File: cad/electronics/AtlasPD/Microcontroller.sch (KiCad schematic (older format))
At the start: 23 parts, among them J2 USB_C_Receptacle_USB2.0, SW1 SW_MEC_5E, U2 ATmega328P-AU, U4 CP2104, Y1 CSTNE16M0V53-R0

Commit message: Started layout
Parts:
- removed SW1: SW_MEC_5E, Button_Switch_SMD:SW_Push_1P1T_NO_6x6mm_H9.5mm, symbol Switch:SW_MEC_5E
- added R12: 0, Resistor_SMD:R_0603_1608Metric, symbol Device:R_Small
- added SW1: SW_SPST, Button_Switch_SMD:SW_Push_1P1T_NO_6x6mm_H9.5mm, symbol Switch:SW_SPST
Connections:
- wire segments 121 -> 117
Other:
- moved on the sheet: R4, R5
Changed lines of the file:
@@
 NoConn ~ 1050 2800
 Wire Wire Line
-	1950 1800 2100 1800
-Wire Wire Line
-	2100 1800 2100 1900
-Wire Wire Line
 	2100 1900 1950 1900
 Wire Wire Line
@@
 Wire Wire Line
 	2100 2100 1950 2100
-Text Label 2450 1800 2    50   ~ 0
+Text Label 2750 1800 2    50   ~ 0
 USB_DN
 Text Label 2450 2000 2    50   ~ 0
 USB_DP
-Wire Wire Line
-	2450 1800 2100 1800
-Connection ~ 2100 1800
 Wire Wire Line
 	2450 2000 2100 2000
@@
 L Device:R_Small R5
 U 1 1 6160033E
-P 2300 1600
-F 0 "R5" V 2300 1600 50  0000 C CNN
-F 1 "5.11K" V 2350 1800 50  0000 C CNN
-F 2 "Resistor_SMD:R_0603_1608Metric" H 2300 1600 50  0001 C CNN
-F 3 "~" H 2300 1600 50  0001 C CNN
-	1    2300 1600
+P 2550 1600
+F 0 "R5" V 2550 1600 50  0000 C CNN
+F 1 "5.11K" V 2600 1800 50  0000 C CNN
+F 2 "Resistor_SMD:R_0603_1608Metric" H 2550 1600 50  0001 C CNN
+F 3 "~" H 2550 1600 50  0001 C CNN
+	1    2550 1600
 	0    1    1    0
 $EndComp
@@
 L Device:R_Small R4
 U 1 1 61600F72
-P 2300 1500
-F 0 "R4" V 2300 1500 50  0000 C CNN
-F 1 "5.11K" V 2250 1700 50  0000 C CNN
-F 2 "Resistor_SMD:R_0603_1608Metric" H 2300 1500 50  0001 C CNN
-F 3 "~" H 2300 1500 50  0001 C CNN
-	1    2300 1500
+P 2550 1500
+F 0 "R4" V 2550 1500 50  0000 C CNN
+F 1 "5.11K" V 2500 1700 50  0000 C CNN
+F 2 "Resistor_SMD:R_0603_1608Metric" H 2550 1500 50  0001 C CNN
+F 3 "~" H 2550 1500 50  0001 C CNN
+	1    2550 1500
 	0    1    1    0
 $EndComp
 Wire Wire Line
-	1950 1500 2200 1500
-Wire Wire Line
-	1950 1600 2200 1600
-Wire Wire Line
-	2400 1600 2650 1600
-Wire Wire Line
-	2650 1600 2650 1500
-Wire Wire Line
-	2650 1500 2400 1500
+	2650 1600 2900 1600
+Wire Wire Line
+	2900 1600 2900 1500
+Wire Wire Line
+	2900 1500 2650 1500
 $Comp
 L power:GND #PWR010
 U 1 1 616032B8
-P 2650 1650
-F 0 "#PWR010" H 2650 1400 50  0001 C CNN
-F 1 "GND" H 2655 1477 50  0000 C CNN
-F 2 "" H 2650 1650 50  0001 C CNN
-F 3 "" H 2650 1650 50  0001 C CNN
-	1    2650 1650
-	1    0    0    -1
-$EndComp
-Wire Wire Line
-	2650 1650 2650 1600
-Connection ~ 2650 1600
+P 2900 1650
+F 0 "#PWR010" H 2900 1400 50  0001 C CNN
+F 1 "GND" H 2905 1477 50  0000 C CNN
+F 2 "" H 2900 1650 50  0001 C CNN
+F 3 "" H 2900 1650 50  0001 C CNN
+	1    2900 1650
+	1    0    0    -1
+$EndComp
+Wire Wire Line
+	2900 1650 2900 1600
+Connection ~ 2900 1600
 NoConn ~ 5100 1000
 NoConn ~ 4200 2300
@@
 TXD
 Text Label 5900 1900 2    50   ~ 0
-TXD
+RXD
 Wire Wire Line
 	5600 1500 5900 1500
@@
 	8650 1550 8800 1550
 $Comp
-L Switch:SW_MEC_5E SW1
-U 1 1 616F3B46
-P 10350 3050
-F 0 "SW1" H 10350 3100 50  0000 C CNN
-F 1 "SW_MEC_5E" H 10750 3200 50  0000 C CNN
-F 2 "Button_Switch_SMD:SW_Push_1P1T_NO_6x6mm_H9.5mm" H 10350 3350 50  0001 C CNN
-F 3 "http://www.apem.com/int/index.php?controller=attachment&id_attachment=1371" H 10350 3350 50  0001 C CNN
-	1    10350 3050
-	1    0    0    -1
-$EndComp
-$Comp
 L Device:Resonator_Small Y1
 U 1 1 616F5A36
@@
 $EndComp
 Wire Wire Line
-	8700 2250 9650 2250
-Wire Wire Line
 	8650 2150 9550 2150
 Wire Wire Line
@@
 Wire Wire Line
 	10550 3050 10700 3050
-Wire Wire Line
-	10550 2950 10700 2950
-Wire Wire Line
-	10700 2950 10700 3050
-Connection ~ 10700 3050
 $Comp
 L Device:R_Small R11
@@
 	-1   0    0    1
 $EndComp
-Wire Wire Line
-	10150 2950 10050 2950
-Wire Wire Line
-	10050 2950 10050 3050
-Connection ~ 10050 3050
-Wire Wire Line
-	10050 3050 10150 3050
 $Comp
 L Device:C_Small C11
@@
 	9850 2900 9850 3050
 Connection ~ 9850 3050
-Wire Wire Line
-	9850 3050 10050 3050
 Wire Wire Line
 	9650 2900 9650 3050
@@
 Wire Wire Line
 	8250 1200 8250 1250
+$Comp
+L Switch:SW_SPST SW1
+U 1 1 61815A6D
+P 10350 3050
+F 0 "SW1" H 10350 3000 50  0000 C CNN
+F 1 "SW_SPST" H 10350 3194 50  0000 C CNN
+F 2 "Button_Switch_SMD:SW_Push_1P1T_NO_6x6mm_H9.5mm" H 10350 3050 50  0001 C CNN
+F 3 "~" H 10350 3050 50  0001 C CNN
+	1    10350 3050
+	1    0    0    -1
+$EndComp
+Wire Wire Line
+	9850 3050 10150 3050
+$Comp
+L Device:R_Small R12
+U 1 1 6182599D
+P 2200 1900
+F 0 "R12" V 2200 1900 50  0000 C CNN
+F 1 "0" V 2150 1800 50  0000 C CNN
+F 2 "Resistor_SMD:R_0603_1608Metric" H 2200 1900 50  0001 C CNN
+F 3 "~" H 2200 1900 50  0001 C CNN
+	1    2200 1900
+	0    1    1    0
+$EndComp
+Wire Wire Line
+	1950 1800 2450 1800
+Wire Wire Line
+	2300 1900 2450 1900
+Wire Wire Line
+	2450 1900 2450 1800
+Wire Wire Line
+	2450 1800 2750 1800
+Connection ~ 2450 1800
+Wire Wire Line
+	1950 1500 2450 1500
+Wire Wire Line
+	1950 1600 2450 1600
+Wire Wire Line
+	8650 2250 9650 2250
 $EndSCHEMATC

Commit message: Layout updates, new PMICs for motors
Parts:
- D3, D4, D5, D6: footprint Capacitor_SMD:C_0603_1608Metric -> LED_SMD:LED_0603_1608Metric
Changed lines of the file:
@@
 F 0 "D4" V 3496 1930 50  0000 R CNN
 F 1 "RED" V 3405 1930 50  0000 R CNN
-F 2 "Capacitor_SMD:C_0603_1608Metric" V 3450 2000 50  0001 C CNN
+F 2 "LED_SMD:LED_0603_1608Metric" V 3450 2000 50  0001 C CNN
 F 3 "~" V 3450 2000 50  0001 C CNN
 	1    3450 2000
@@
 F 0 "D3" V 3250 2250 50  0000 R CNN
 F 1 "RED" V 3150 2250 50  0000 R CNN
-F 2 "Capacitor_SMD:C_0603_1608Metric" V 3300 2100 50  0001 C CNN
+F 2 "LED_SMD:LED_0603_1608Metric" V 3300 2100 50  0001 C CNN
 F 3 "~" V 3300 2100 50  0001 C CNN
 	1    3300 2100
@@
 F 0 "D5" V 4789 5132 50  0000 R CNN
 F 1 "YELLOW" V 4698 5132 50  0000 R CNN
-F 2 "Capacitor_SMD:C_0603_1608Metric" H 4750 5250 50  0001 C CNN
+F 2 "LED_SMD:LED_0603_1608Metric" H 4750 5250 50  0001 C CNN
 F 3 "~" H 4750 5250 50  0001 C CNN
 	1    4750 5250
@@
 F 0 "D6" V 5489 5132 50  0000 R CNN
 F 1 "GREEN" V 5398 5132 50  0000 R CNN
-F 2 "Capacitor_SMD:C_0603_1608Metric" H 5450 5250 50  0001 C CNN
+F 2 "LED_SMD:LED_0603_1608Metric" H 5450 5250 50  0001 C CNN
 F 3 "~" H 5450 5250 50  0001 C CNN
 	1    5450 5250

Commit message: Found a bug, squashed it
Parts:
- added J1: Barrel_Jack_MountingPin, Connector_BarrelJack:BarrelJack_Horizontal, symbol Connector:Barrel_Jack_MountingPin
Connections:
- net labels added: EN_MTRS
- wire segments 117 -> 122
- no-connect marks 16 -> 17
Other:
- note added: "ATMEGA328P Microcontroller"
- note added: "DC Barrel Jack 5V Input"
- note added: "Design Block Interconnects"
- note added: "IO Voltage Level Selector"
- note added: "Status LEDs"
- note added: "USB Type-C Connector"
- note added: "USB to UART Serial Bridge"
- moved on the sheet: C6, C7, D3, D4, D5, D6, JP1, R6, R7, R8, R9, U4

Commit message: First Board Layout done
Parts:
- removed J1: Barrel_Jack_MountingPin, Connector_BarrelJack:BarrelJack_Horizontal, symbol Connector:Barrel_Jack_MountingPin
- added J1: Conn_01x04, Connector_JST:JST_PH_B4B-PH-K_1x04_P2.00mm_Vertical, symbol Connector_Generic:Conn_01x04
- renumbered C7 to C1, C6 to C2, C9 to C3, C10 to C4, C11 to C5, D5 to D1, D3 to D2, D4 to D3, D6 to D4, R12 to R1, R4 to R2, R5 to R3, R8 to R4, R6 to R5, R7 to R6, R9 to R7, R10 to R8, R11 to R9, U4 to U1
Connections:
- net labels added: +BATT
- wire segments 122 -> 130
- no-connect marks 17 -> 16
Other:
- note added: "Power Port"
- note removed: "DC Barrel Jack 5V Input"
- moved on the sheet: C3, C4

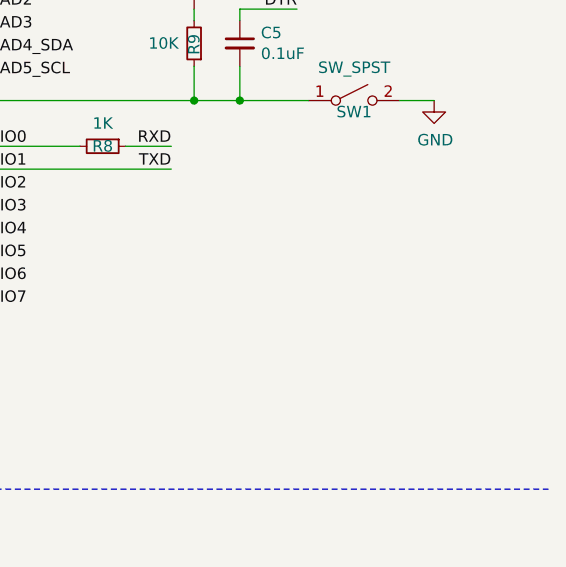
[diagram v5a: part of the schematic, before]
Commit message: Additional layout chaneges, and added testpoints
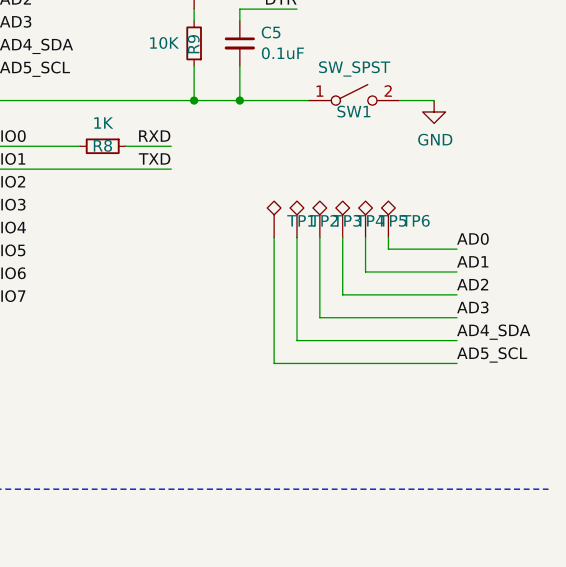
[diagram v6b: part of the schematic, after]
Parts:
- added TP1, TP2, TP3, TP4, TP5, TP6: TestPoint_Alt, TestPoint:TestPoint_Pad_D1.0mm, symbol Connector:TestPoint_Alt
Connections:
- net AD0: now also TP6.1
- net AD1: now also TP5.1
- net AD2: now also TP4.1
- net AD3: now also TP3.1
- net AD4_SDA: now also TP2.1
- net AD5_SCL: now also TP1.1
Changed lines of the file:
@@
 	8800 1200 8650 1200
 NoConn ~ 1050 2800
+$Comp
+L Connector:TestPoint_Alt TP1
+U 1 1 617127E7
+P 10000 3650
+F 0 "TP1" H 10058 3722 50  0000 L CNN
+F 1 "TestPoint_Alt" H 10058 3677 50  0001 L CNN
+F 2 "TestPoint:TestPoint_Pad_D1.0mm" H 10200 3650 50  0001 C CNN
+F 3 "~" H 10200 3650 50  0001 C CNN
+	1    10000 3650
+	1    0    0    -1
+$EndComp
+$Comp
+L Connector:TestPoint_Alt TP2
+U 1 1 61713F79
+P 10100 3650
+F 0 "TP2" H 10158 3722 50  0000 L CNN
+F 1 "TestPoint_Alt" H 10158 3677 50  0001 L CNN
+F 2 "TestPoint:TestPoint_Pad_D1.0mm" H 10300 3650 50  0001 C CNN
+F 3 "~" H 10300 3650 50  0001 C CNN
+	1    10100 3650
+	1    0    0    -1
+$EndComp
+$Comp
+L Connector:TestPoint_Alt TP3
+U 1 1 61714148
+P 10200 3650
+F 0 "TP3" H 10258 3722 50  0000 L CNN
+F 1 "TestPoint_Alt" H 10258 3677 50  0001 L CNN
+F 2 "TestPoint:TestPoint_Pad_D1.0mm" H 10400 3650 50  0001 C CNN
+F 3 "~" H 10400 3650 50  0001 C CNN
+	1    10200 3650
+	1    0    0    -1
+$EndComp
+$Comp
+L Connector:TestPoint_Alt TP4
+U 1 1 61714471
+P 10300 3650
+F 0 "TP4" H 10358 3722 50  0000 L CNN
+F 1 "TestPoint_Alt" H 10358 3677 50  0001 L CNN
+F 2 "TestPoint:TestPoint_Pad_D1.0mm" H 10500 3650 50  0001 C CNN
+F 3 "~" H 10500 3650 50  0001 C CNN
+	1    10300 3650
+	1    0    0    -1
+$EndComp
+$Comp
+L Connector:TestPoint_Alt TP5
+U 1 1 61714782
+P 10400 3650
+F 0 "TP5" H 10458 3722 50  0000 L CNN
+F 1 "TestPoint_Alt" H 10458 3677 50  0001 L CNN
+F 2 "TestPoint:TestPoint_Pad_D1.0mm" H 10600 3650 50  0001 C CNN
+F 3 "~" H 10600 3650 50  0001 C CNN
+	1    10400 3650
+	1    0    0    -1
+$EndComp
+$Comp
+L Connector:TestPoint_Alt TP6
+U 1 1 617149A7
+P 10500 3650
+F 0 "TP6" H 10558 3722 50  0000 L CNN
+F 1 "TestPoint_Alt" H 10558 3677 50  0001 L CNN
+F 2 "TestPoint:TestPoint_Pad_D1.0mm" H 10700 3650 50  0001 C CNN
+F 3 "~" H 10700 3650 50  0001 C CNN
+	1    10500 3650
+	1    0    0    -1
+$EndComp
+Text Label 10800 4200 0    50   ~ 0
+AD5_SCL
+Text Label 10800 4100 0    50   ~ 0
+AD4_SDA
+Text Label 10800 4000 0    50   ~ 0
+AD3
+Text Label 10800 3900 0    50   ~ 0
+AD2
+Text Label 10800 3800 0    50   ~ 0
+AD1
+Text Label 10800 3700 0    50   ~ 0
+AD0
+Wire Wire Line
+	10500 3650 10500 3700
+Wire Wire Line
+	10500 3700 10800 3700
+Wire Wire Line
+	10400 3650 10400 3800
+Wire Wire Line
+	10400 3800 10800 3800
+Wire Wire Line
+	10300 3650 10300 3900
+Wire Wire Line
+	10300 3900 10800 3900
+Wire Wire Line
+	10200 4000 10200 3650
+Wire Wire Line
+	10200 4000 10800 4000
+Wire Wire Line
+	10100 3650 10100 4100
+Wire Wire Line
+	10100 4100 10800 4100
+Wire Wire Line
+	10000 4200 10000 3650
+Wire Wire Line
+	10000 4200 10800 4200
 $EndSCHEMATC

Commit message: Layout updates
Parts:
- added TP207, TP208, TP209, TP210, TP211, TP212: TestPoint_Alt, TestPoint:TestPoint_Pad_D1.0mm, symbol Connector:TestPoint_Alt
- renumbered C1 to C201, C2 to C202, C3 to C203, C4 to C204, C5 to C205, D1 to D201, D2 to D202, D3 to D203, D4 to D204, J2 to J201, J1 to J202, JP1 to JP201, R1 to R201, R2 to R202, R3 to R203, R4 to R204, R5 to R205, R6 to R206, R7 to R207, R8 to R208, R9 to R209, SW1 to SW201, TP1 to TP201, TP2 to TP202, TP3 to TP203, TP4 to TP204, TP5 to TP205, TP6 to TP206, U1 to U201, U2 to U202, Y1 to Y201
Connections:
- net EN_MTRS: now also TP209.1
- net GND: now also TP207.1
- net IO12_MISO: now also TP210.1
- net S4: now also TP211.1
- net VCC: now also TP212.1
- net RESET: now reaches C205.2, R209.1, SW201.1 (A), U202.29 (~RESET~/PC6)
- net RESET: now also TP208.1
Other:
- note added: "ICSP Pads"
- note added: "Unused MCU pins"

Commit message: Preliminary PCB Production files
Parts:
- C201, C203, C204, C205: LCSC (none) -> C14663; LCSC Part # (none) -> C14663
- C202: LCSC (none) -> C96446; LCSC Part # (none) -> C96446
- D201: LCSC (none) -> C72038; LCSC Part # (none) -> C72038
- D202, D203: LCSC (none) -> C2286; LCSC Part # (none) -> C2286
- D204: LCSC (none) -> C72043; LCSC Part # (none) -> C72043
- J201: LCSC (none) -> C165948; LCSC Part # (none) -> C165948
- R202, R203: LCSC (none) -> C112314; LCSC Part # (none) -> C112314
- R204, R207: value R -> 1k; LCSC (none) -> C21190; LCSC Part # (none) -> C21190
- R205, R206, R208: LCSC (none) -> C21190; LCSC Part # (none) -> C21190
- R209: LCSC (none) -> C25804; LCSC Part # (none) -> C25804
- SW201: LCSC (none) -> C318884; LCSC Part # (none) -> C318884
- U201: LCSC (none) -> C47742; LCSC Part # (none) -> C47742
- U202: LCSC (none) -> C14877; LCSC Part # (none) -> C14877
- Y201: LCSC (none) -> C341521; LCSC Part # (none) -> C341521
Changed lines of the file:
@@
 F 2 "Package_QFP:TQFP-32_7x7mm_P0.8mm" H 8050 2750 50  0001 C CIN
 F 3 "http://ww1.microchip.com/downloads/en/DeviceDoc/ATmega328_P%20AVR%20MCU%20with%20picoPower%20Technology%20Data%20Sheet%2040001984A.pdf" H 8050 2750 50  0001 C CNN
+F 4 "C14877" H 8050 2750 50  0001 C CNN "LCSC Part #"
+F 5 "C14877" H 8050 2750 50  0001 C CNN "LCSC"
 	1    8050 2750
 	1    0    0    -1
@@
 F 2 "Connector_USB:USB_C_Receptacle_HRO_TYPE-C-31-M-12" H 1500 1900 50  0001 C CNN
 F 3 "https://www.usb.org/sites/default/files/documents/usb_type-c.zip" H 1500 1900 50  0001 C CNN
+F 4 "C165948" H 1350 1900 50  0001 C CNN "LCSC Part #"
+F 5 "C165948" H 1350 1900 50  0001 C CNN "LCSC"
 	1    1350 1900
 	1    0    0    -1
@@
 F 2 "Resistor_SMD:R_0603_1608Metric" H 2550 1600 50  0001 C CNN
 F 3 "~" H 2550 1600 50  0001 C CNN
+F 4 "C112314" H 2550 1600 50  0001 C CNN "LCSC Part #"
+F 5 "C112314" H 2550 1600 50  0001 C CNN "LCSC"
 	1    2550 1600
 	0    1    1    0
@@
 F 2 "Resistor_SMD:R_0603_1608Metric" H 2550 1500 50  0001 C CNN
 F 3 "~" H 2550 1500 50  0001 C CNN
+F 4 "C112314" H 2550 1500 50  0001 C CNN "LCSC Part #"
+F 5 "C112314" H 2550 1500 50  0001 C CNN "LCSC"
 	1    2550 1500
 	0    1    1    0
@@
 F 2 "LED_SMD:LED_0603_1608Metric" V 3850 2050 50  0001 C CNN
 F 3 "~" V 3850 2050 50  0001 C CNN
+F 4 "C2286" H 3850 2050 50  0001 C CNN "LCSC Part #"
+F 5 "C2286" H 3850 2050 50  0001 C CNN "LCSC"
 	1    3850 2050
 	0    -1   -1   0
@@
 F 2 "LED_SMD:LED_0603_1608Metric" V 3700 2150 50  0001 C CNN
 F 3 "~" V 3700 2150 50  0001 C CNN
+F 4 "C2286" H 3700 2150 50  0001 C CNN "LCSC Part #"
+F 5 "C2286" H 3700 2150 50  0001 C CNN "LCSC"
 	1    3700 2150
 	0    -1   -1   0
@@
 F 2 "Resistor_SMD:R_0603_1608Metric" H 4100 2250 50  0001 C CNN
 F 3 "~" H 4100 2250 50  0001 C CNN
+F 4 "C21190" H 4100 2250 50  0001 C CNN "LCSC Part #"
+F 5 "C21190" H 4100 2250 50  0001 C CNN "LCSC"
 	1    4100 2250
 	0    1    1    0
@@
 F 2 "Resistor_SMD:R_0603_1608Metric" H 4300 2150 50  0001 C CNN
 F 3 "~" H 4300 2150 50  0001 C CNN
+F 4 "C21190" H 4300 2150 50  0001 C CNN "LCSC Part #"
+F 5 "C21190" H 4300 2150 50  0001 C CNN "LCSC"
 	1    4300 2150
 	0    1    1    0
@@
 F 2 "Capacitor_SMD:C_0603_1608Metric" H 4350 2850 50  0001 C CNN
 F 3 "~" H 4350 2850 50  0001 C CNN
+F 4 "C96446" H 4350 2850 50  0001 C CNN "LCSC Part #"
+F 5 "C96446" H 4350 2850 50  0001 C CNN "LCSC"
 	1    4350 2850
 	-1   0    0    1
@@
 F 2 "Package_DFN_QFN:QFN-24-1EP_4x4mm_P0.5mm_EP2.6x2.6mm" H 5450 1000 50  0001 L CNN
 F 3 "https://www.silabs.com/documents/public/data-sheets/cp2104.pdf" H 4750 3200 50  0001 C CNN
+F 4 "C47742" H 5300 1950 50  0001 C CNN "LCSC Part #"
+F 5 "C47742" H 5300 1950 50  0001 C CNN "LCSC"
 	1    5300 1950
 	1    0    0    -1
@@
 F 2 "Capacitor_SMD:C_0603_1608Metric" H 4100 1150 50  0001 C CNN
 F 3 "~" H 4100 1150 50  0001 C CNN
+F 4 "C14663" H 4100 1150 50  0001 C CNN "LCSC Part #"
+F 5 "C14663" H 4100 1150 50  0001 C CNN "LCSC"
 	1    4100 1150
 	-1   0    0    1
@@
 F 2 "Capacitor_SMD:C_0603_1608Metric" H 8650 1100 50  0001 C CNN
 F 3 "~" H 8650 1100 50  0001 C CNN
+F 4 "C14663" H 8650 1100 50  0001 C CNN "LCSC Part #"
+F 5 "C14663" H 8650 1100 50  0001 C CNN "LCSC"
 	1    8650 1100
 	-1   0    0    1
@@
 F 2 "Capacitor_SMD:C_0603_1608Metric" H 8950 1100 50  0001 C CNN
 F 3 "~" H 8950 1100 50  0001 C CNN
+F 4 "C14663" H 8950 1100 50  0001 C CNN "LCSC Part #"
+F 5 "C14663" H 8950 1100 50  0001 C CNN "LCSC"
 	1    8950 1100
 	-1   0    0    1
@@
 F 2 "SamacSys_Parts:CSTNE16M0V530000R0" H 9725 2150 50  0001 C CNN
 F 3 "~" H 9725 2150 50  0001 C CNN
+F 4 "C341521" H 9750 2150 50  0001 C CNN "LCSC Part #"
+F 5 "C341521" H 9750 2150 50  0001 C CNN "LCSC"
 	1    9750 2150
 	0    -1   -1   0
@@
 F 2 "Resistor_SMD:R_0603_1608Metric" H 9650 2800 50  0001 C CNN
 F 3 "~" H 9650 2800 50  0001 C CNN
+F 4 "C25804" H 9650 2800 50  0001 C CNN "LCSC Part #"
+F 5 "C25804" H 9650 2800 50  0001 C CNN "LCSC"
 	1    9650 2800
 	-1   0    0    1
@@
 F 2 "Capacitor_SMD:C_0603_1608Metric" H 9850 2800 50  0001 C CNN
 F 3 "~" H 9850 2800 50  0001 C CNN
+F 4 "C14663" H 9850 2800 50  0001 C CNN "LCSC Part #"
+F 5 "C14663" H 9850 2800 50  0001 C CNN "LCSC"
 	1    9850 2800
 	1    0    0    -1
@@
 F 2 "Resistor_SMD:R_0603_1608Metric" H 9250 3250 50  0001 C CNN
 F 3 "~" H 9250 3250 50  0001 C CNN
+F 4 "C21190" H 9250 3250 50  0001 C CNN "LCSC Part #"
+F 5 "C21190" H 9250 3250 50  0001 C CNN "LCSC"
 	1    9250 3250
 	0    1    1    0
@@
 F 2 "LED_SMD:LED_0603_1608Metric" H 3650 4750 50  0001 C CNN
 F 3 "~" H 3650 4750 50  0001 C CNN
+F 4 "C72038" H 3650 4750 50  0001 C CNN "LCSC Part #"
+F 5 "C72038" H 3650 4750 50  0001 C CNN "LCSC"
 	1    3650 4750
 	0    -1   -1   0
@@
 F 2 "LED_SMD:LED_0603_1608Metric" H 4350 4750 50  0001 C CNN
 F 3 "~" H 4350 4750 50  0001 C CNN
+F 4 "C72043" H 4350 4750 50  0001 C CNN "LCSC Part #"
+F 5 "C72043" H 4350 4750 50  0001 C CNN "LCSC"
 	1    4350 4750
 	0    -1   -1   0
@@
 P 3650 5150
 F 0 "R204" H 3720 5196 50  0000 L CNN
-F 1 "R" H 3720 5105 50  0000 L CNN
+F 1 "1k" H 3720 5105 50  0000 L CNN
 F 2 "Resistor_SMD:R_0603_1608Metric" V 3580 5150 50  0001 C CNN
 F 3 "~" H 3650 5150 50  0001 C CNN
+F 4 "C21190" H 3650 5150 50  0001 C CNN "LCSC Part #"
+F 5 "C21190" H 3650 5150 50  0001 C CNN "LCSC"
 	1    3650 5150
 	1    0    0    -1
@@
 P 4350 5150
 F 0 "R207" H 4420 5196 50  0000 L CNN
-F 1 "R" H 4420 5105 50  0000 L CNN
+F 1 "1k" H 4420 5105 50  0000 L CNN
 F 2 "Resistor_SMD:R_0603_1608Metric" V 4280 5150 50  0001 C CNN
 F 3 "~" H 4350 5150 50  0001 C CNN
+F 4 "C21190" H 4350 5150 50  0001 C CNN "LCSC Part #"
+F 5 "C21190" H 4350 5150 50  0001 C CNN "LCSC"
 	1    4350 5150
 	1    0    0    -1
@@
 F 2 "Button_Switch_SMD:SW_Push_1P1T_NO_6x6mm_H9.5mm" H 10350 3050 50  0001 C CNN
 F 3 "~" H 10350 3050 50  0001 C CNN
+F 4 "C318884" H 10350 3050 50  0001 C CNN "LCSC Part #"
+F 5 "C318884" H 10350 3050 50  0001 C CNN "LCSC"
 	1    10350 3050
 	1    0    0    -1
